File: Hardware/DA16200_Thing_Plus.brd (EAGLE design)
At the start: 22.9 x 58.4 mm, 98 parts, among them J2 THING_PLUS, J3 Qwiic, J5 USB C, J6 microSD, J7 CORTEX_JTAG_DEBUG_PTH_NS, Q1 20V/4.2A/52mΩ/1.4W, U1 DA16200MOD, U2 CH340E_MSOP10, U3 MCP73831, U5 4MB Flash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

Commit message: Checklist
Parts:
- added R20, R21: 10k, SparkFun-Resistors:0402-TIGHT
- renumbered JP2 to LED, JP3 to CHG
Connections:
- net 3.3V: now also R20.2, R21.2
- net SD_CS: now also R21.1
- net SPI_CSB: now also R20.1
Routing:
- net 3.3V: track 20.9 -> 22.4 mm, vias 12 -> 14
- net SPI_CSB: track 22.4 -> 23.7 mm
- net SD_CS: track 48.9 -> 50.0 mm
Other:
- board text added: "1"
- board text added: "2"
- board text added: "3"
- board text added: "4"
- board text added: "Four Layers"
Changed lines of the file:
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@@
 <?xml version="1.0" encoding="utf-8"?>
 <!DOCTYPE eagle SYSTEM "eagle.dtd">
-<eagle version="9.6.2">
+<eagle version="9.5.2">
 <drawing>
 <settings>
@@
 <layer number="37" name="tTest" color="7" fill="1" visible="no" active="yes"/>
 <layer number="38" name="bTest" color="7" fill="1" visible="no" active="yes"/>
-<layer number="39" name="tKeepout" color="4" fill="11" visible="no" active="yes"/>
+<layer number="39" name="tKeepout" color="4" fill="11" visible="yes" active="yes"/>
 <layer number="40" name="bKeepout" color="1" fill="11" visible="no" active="yes"/>
 <layer number="41" name="tRestrict" color="4" fill="10" visible="no" active="yes"/>
@@
 <layer number="45" name="Holes" color="7" fill="1" visible="yes" active="yes"/>
 <layer number="46" name="Milling" color="3" fill="1" visible="no" active="yes"/>
-<layer number="47" name="Measures" color="7" fill="1" visible="no" active="yes"/>
+<layer number="47" name="Measures" color="7" fill="1" visible="yes" active="yes"/>
 <layer number="48" name="Document" color="7" fill="1" visible="no" active="yes"/>
 <layer number="49" name="Reference" color="7" fill="1" visible="no" active="yes"/>
@@
 <layer number="95" name="Names" color="7" fill="1" visible="no" active="no"/>
 <layer number="96" name="Values" color="7" fill="1" visible="no" active="no"/>
-<layer number="2" name="gndvert" color="10" fill="7" visible="no" active="yes"/>
-<layer number="15" name="pwrhorz" color="4" fill="7" visible="no" active="yes"/>
+<layer number="2" name="gndvert" color="10" fill="7" visible="yes" active="yes"/>
+<layer number="15" name="pwrhorz" color="4" fill="7" visible="yes" active="yes"/>
 <layer number="3" name="Route3" color="4" fill="3" visible="no" active="no"/>
 <layer number="4" name="Route4" color="1" fill="4" visible="no" active="no"/>
@@
 <text x="8.255" y="15.24" size="1.27" layer="21" font="vector" ratio="15" rot="R90">-</text>
 <text x="13.081" y="-19.177" size="1.778" layer="51" font="vector" ratio="15">Priyanka Makin</text>
+<text x="15.24" y="55.88" size="1.778" layer="1" font="vector" ratio="15">1</text>
+<text x="16.51" y="55.88" size="1.778" layer="2" font="vector" ratio="15">2</text>
+<text x="15.24" y="53.34" size="1.778" layer="15" font="vector" ratio="15">3</text>
+<text x="17.78" y="53.34" size="1.778" layer="16" font="vector" ratio="15" rot="MR0">4</text>
+<text x="48.641" y="44.323" size="1.778" layer="51" font="vector" ratio="15">Four Layers</text>
 </plain>
 <attributes>
@@
 <attribute name="VALUE" x="4.953" y="33.02" size="0.6096" layer="27" font="vector" ratio="20" rot="R270" align="top-center"/>
 </element>
-<element name="JP2" library="SparkFun-Jumpers" package="SMT-JUMPER_2_NC_TRACE_SILK" package3d_urn="urn:adsk.eagle:package:39281/1" value="JUMPER-SMT_2_NC_TRACE_SILK" x="19.05" y="6.35" smashed="yes" rot="MR180">
+<element name="LED" library="SparkFun-Jumpers" package="SMT-JUMPER_2_NC_TRACE_SILK" package3d_urn="urn:adsk.eagle:package:39281/1" value="JUMPER-SMT_2_NC_TRACE_SILK" x="19.05" y="6.35" smashed="yes" rot="MR180">
 <attribute name="NAME" x="19.05" y="5.207" size="0.6096" layer="26" font="vector" ratio="20" rot="MR180" align="bottom-center"/>
 <attribute name="VALUE" x="19.05" y="7.493" size="0.6096" layer="28" font="vector" ratio="20" rot="MR180" align="top-center"/>
@@
 <attribute name="PROD_ID" value="RES-15550" x="19.685" y="13.724" size="1.778" layer="27" font="vector" ratio="15" rot="R90" display="off"/>
 </element>
-<element name="JP3" library="SparkFun-Jumpers" package="SMT-JUMPER_3_1-NC_TRACE_SILK" package3d_urn="urn:adsk.eagle:package:39288/1" value="JUMPER-SMT_3_1-NC_TRACE_SILK" x="12.319" y="27.178" smashed="yes" rot="MR270">
+<element name="CHG" library="SparkFun-Jumpers" package="SMT-JUMPER_3_1-NC_TRACE_SILK" package3d_urn="urn:adsk.eagle:package:39288/1" value="JUMPER-SMT_3_1-NC_TRACE_SILK" x="12.319" y="27.178" smashed="yes" rot="MR270">
 <attribute name="NAME" x="11.176" y="25.908" size="0.6096" layer="26" font="vector" ratio="20" rot="MR270" align="bottom-center"/>
 <attribute name="VALUE" x="13.462" y="25.908" size="0.6096" layer="28" font="vector" ratio="20" rot="MR270" align="top-center"/>
@@
 <element name="U$4" library="output" package="#CURR_#0" value="" x="18.288" y="23.622" smashed="yes" rot="MR0"/>
 <element name="U$5" library="output" package="##RST##0" value="" x="21.209" y="13.97" smashed="yes" rot="MR0"/>
+<element name="R20" library="SparkFun-Resistors" package="0402-TIGHT" value="10k" x="8.763" y="47.752" smashed="yes" rot="MR90">
+<attribute name="NAME" x="9.325" y="47.752" size="0.6096" layer="26" font="vector" ratio="20" rot="MR90" align="bottom-center"/>
+<attribute name="PROD_ID" value="RES-14241" x="8.763" y="47.752" size="1.778" layer="28" font="vector" ratio="15" rot="MR90" display="off"/>
+<attribute name="VALUE" x="8.201" y="47.752" size="0.6096" layer="28" font="vector" ratio="20" rot="MR90" align="top-center"/>
+</element>
+<element name="R21" library="SparkFun-Resistors" package="0402-TIGHT" value="10k" x="16.51" y="33.02" smashed="yes" rot="MR180">
+<attribute name="NAME" x="16.51" y="32.458" size="0.6096" layer="26" font="vector" ratio="20" rot="MR180" align="bottom-center"/>
+<attribute name="PROD_ID" value="RES-14241" x="16.51" y="33.02" size="1.778" layer="28" font="vector" ratio="15" rot="MR180" display="off"/>
+<attribute name="VALUE" x="16.51" y="33.582" size="0.6096" layer="28" font="vector" ratio="20" rot="MR180" align="top-center"/>
+</element>
 </elements>
 <signals>
@@
 <contactref element="J7" pad="1"/>
 <contactref element="R9" pad="1"/>
-<contactref element="JP2" pad="2"/>
+<contactref element="LED" pad="2"/>
 <polygon width="0.1778" layer="15" isolate="0.3048">
 <vertex x="0" y="0"/>
@@
 <wire x1="19.5707" y1="6.35" x2="19.5707" y2="8.3693" width="0.3048" layer="16"/>
 <wire x1="19.5707" y1="8.3693" x2="19.05" y2="8.89" width="0.3048" layer="16"/>
+<contactref element="R21" pad="2"/>
+<contactref element="R20" pad="2"/>
+<wire x1="8.763" y1="48.252" x2="8.763" y2="49.022" width="0.3048" layer="16"/>
+<via x="8.763" y="49.022" extent="1-16" drill="0.3048"/>
+<wire x1="17.01" y1="33.02" x2="17.78" y2="33.02" width="0.3048" layer="16"/>
+<via x="17.78" y="33.02" extent="1-16" drill="0.3048"/>
 </signal>
 <signal name="GND">
@@
 <signal name="N$14">
 <contactref element="U3" pad="5"/>
-<contactref element="JP3" pad="2"/>
+<contactref element="CHG" pad="2"/>
 <wire x1="14.4479" y1="24.704" x2="14.351" y2="24.8009" width="0.1778" layer="1"/>
 <wire x1="14.351" y1="24.8009" x2="14.351" y2="25.527" width="0.1778" layer="1"/>
@@
 <wire x1="2.286" y1="45.974" x2="1.27" y2="46.99" width="0.1778" layer="15"/>
 <wire x1="15.7861" y1="40.386" x2="10.033" y2="40.386" width="0.1778" layer="16"/>
+<contactref element="R20" pad="1"/>
+<wire x1="8.763" y1="45.974" x2="8.763" y2="47.252" width="0.1778" layer="16"/>
 </signal>
 <signal name="SD_CS">
@@
 <wire x1="14.9681" y1="34.163" x2="14.9681" y2="33.7872" width="0.1778" layer="16"/>
 <wire x1="14.9681" y1="33.7872" x2="14.9655" y2="33.7846" width="0.1778" layer="16"/>
-<wire x1="14.9655" y1="33.7846" x2="14.9655" y2="17.018" width="0.1778" layer="16"/>
+<wire x1="14.9655" y1="33.7846" x2="14.9655" y2="33.02" width="0.1778" layer="16"/>
+<wire x1="14.9655" y1="33.02" x2="14.9655" y2="17.018" width="0.1778" layer="16"/>
 <wire x1="14.9655" y1="17.018" x2="14.0425" y2="16.095" width="0.1778" layer="16"/>
 <wire x1="14.0425" y1="16.095" x2="6.21" y2="16.095" width="0.1778" layer="16"/>
+<contactref element="R21" pad="1"/>
+<wire x1="16.01" y1="33.02" x2="14.9655" y2="33.02" width="0.1778" layer="16"/>
 </signal>
 <signal name="GPIOC7">
@@
 <wire x1="6.858" y1="43.18" x2="5.9309" y2="44.1071" width="0.1778" layer="2"/>
 <wire x1="5.9309" y1="44.196" x2="5.9309" y2="44.1071" width="0.1778" layer="2"/>
-<wire x1="6.858" y1="43.18" x2="6.858" y2="30.099" width="0.1778" layer="2"/>
-<wire x1="6.858" y1="30.099" x2="7.747" y2="29.21" width="0.1778" layer="2"/>
+<wire x1="6.858" y1="43.18" x2="6.858" y2="31.75" width="0.1778" layer="2"/>
+<wire x1="7.747" y1="30.861" x2="6.858" y2="31.75" width="0.1778" layer="2"/>
+<wire x1="7.747" y1="30.861" x2="7.747" y2="29.21" width="0.1778" layer="2"/>
 </signal>
 <signal name="TCLK">
@@
 <wire x1="6.163" y1="43.24" x2="6.223" y2="43.18" width="0.1778" layer="1"/>
 <via x="6.223" y="43.18" extent="1-16" drill="0.3048"/>
-<wire x1="7.747" y1="27.94" x2="6.4135" y2="29.2735" width="0.1778" layer="2"/>
-<wire x1="6.4135" y1="42.9895" x2="6.4135" y2="29.2735" width="0.1778" layer="2"/>
+<wire x1="7.747" y1="27.94" x2="7.112" y2="28.575" width="0.1778" layer="2"/>
+<wire x1="7.112" y1="30.734" x2="7.112" y2="28.575" width="0.1778" layer="2"/>
+<wire x1="7.112" y1="30.734" x2="6.4135" y2="31.4325" width="0.1778" layer="2"/>
+<wire x1="6.4135" y1="42.9895" x2="6.4135" y2="31.4325" width="0.1778" layer="2"/>
 <wire x1="6.223" y1="43.18" x2="6.4135" y2="42.9895" width="0.1778" layer="2"/>
 </signal>
@@
 <signal name="N$4">
 <contactref element="D3" pad="A"/>
-<contactref element="JP2" pad="1"/>
+<contactref element="LED" pad="1"/>
 <wire x1="18.173" y1="6.35" x2="17.145" y2="6.35" width="0.1778" layer="1"/>
 <via x="17.145" y="6.35" extent="1-16" drill="0.3048"/>
@@
 </signal>
 <signal name="N$10">
-<contactref element="JP3" pad="3"/>
+<contactref element="CHG" pad="3"/>
 <contactref element="R6" pad="2"/>
 <wire x1="10.66" y1="26.162" x2="12.2936" y2="26.162" width="0.1778" layer="16"/>
@@
 </signal>
 <signal name="N$20">
-<contactref element="JP3" pad="1"/>
+<contactref element="CHG" pad="1"/>
 <contactref element="R14" pad="2"/>
 <wire x1="10.668" y1="28.194" x2="12.2936" y2="28.194" width="0.1778" layer="16"/>

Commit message: Design review
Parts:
- R13: value 200OHM-0402T-1/16W-1% -> 200
- renumbered JP4 to SHLD
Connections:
- net HDR_RTC_WAKE2: no longer C3.1, R5.2
- net RTC_PWR_KEY: now also C3.1
- net RTC_WAKE1: now also R5.2
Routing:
- net HDR_RTC_WAKE2: track 9.80 -> 4.11 mm
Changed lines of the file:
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@@
 <text x="8.255" y="15.24" size="1.27" layer="21" font="vector" ratio="15" rot="R90">-</text>
 <text x="13.081" y="-19.177" size="1.778" layer="51" font="vector" ratio="15">Priyanka Makin</text>
-<text x="15.24" y="55.88" size="1.778" layer="1" font="vector" ratio="15">1</text>
-<text x="16.51" y="55.88" size="1.778" layer="2" font="vector" ratio="15">2</text>
-<text x="15.24" y="53.34" size="1.778" layer="15" font="vector" ratio="15">3</text>
-<text x="17.78" y="53.34" size="1.778" layer="16" font="vector" ratio="15" rot="MR0">4</text>
+<text x="19.05" y="55.88" size="1.778" layer="1" font="vector" ratio="15">1</text>
+<text x="20.32" y="55.88" size="1.778" layer="2" font="vector" ratio="15">2</text>
+<text x="19.05" y="53.34" size="1.778" layer="15" font="vector" ratio="15">3</text>
+<text x="21.59" y="53.34" size="1.778" layer="16" font="vector" ratio="15" rot="MR0">4</text>
 <text x="48.641" y="44.323" size="1.778" layer="51" font="vector" ratio="15">Four Layers</text>
 </plain>
@@
 <attribute name="PROD_ID" value="RES-15238" x="12.708" y="9.652" size="1.778" layer="27" font="vector" ratio="15" display="off"/>
 </element>
-<element name="R13" library="SparkFun-Resistors" package="0402-TIGHT" value="200OHM-0402T-1/16W-1%" x="19.685" y="13.724" smashed="yes" rot="R90">
+<element name="R13" library="SparkFun-Resistors" package="0402-TIGHT" value="200" x="19.685" y="13.724" smashed="yes" rot="R90">
 <attribute name="NAME" x="18.923" y="13.724" size="0.6096" layer="25" font="vector" ratio="20" rot="R90" align="bottom-center"/>
 <attribute name="PROD_ID" value="RES-15550" x="19.685" y="13.724" size="1.778" layer="27" font="vector" ratio="15" rot="R90" display="off"/>
@@
 <attribute name="VALUE" x="15.375" y="13.462" size="0.6096" layer="27" font="vector" ratio="20" align="top-center"/>
 </element>
-<element name="JP4" library="SparkFun-Jumpers" package="SMT-JUMPER_2_NO_SILK" package3d_urn="urn:adsk.eagle:package:39279/1" value="JUMPER-SMT_2_NO_SILK" x="8.89" y="1.27" smashed="yes" rot="MR0">
+<element name="SHLD" library="SparkFun-Jumpers" package="SMT-JUMPER_2_NO_SILK" package3d_urn="urn:adsk.eagle:package:39279/1" value="JUMPER-SMT_2_NO_SILK" x="8.89" y="1.27" smashed="yes" rot="MR0">
 <attribute name="NAME" x="8.89" y="2.413" size="0.6096" layer="26" font="vector" ratio="20" rot="MR0" align="bottom-center"/>
 <attribute name="VALUE" x="8.89" y="0.127" size="0.6096" layer="28" font="vector" ratio="20" rot="MR0" align="top-center"/>
@@
 <contactref element="D5" pad="2"/>
 <contactref element="R14" pad="1"/>
-<contactref element="JP4" pad="1"/>
+<contactref element="SHLD" pad="1"/>
 <contactref element="R4" pad="2"/>
 <contactref element="R1" pad="2"/>
@@
 <wire x1="1.27" y1="39.37" x2="2.032" y2="39.37" width="0.1778" layer="16"/>
 <wire x1="6.35" y1="48.26" x2="3.429" y2="48.26" width="0.1778" layer="16"/>
+<contactref element="C3" pad="1"/>
+<wire x1="5.715" y1="33.52" x2="1.27" y2="39.37" width="0" layer="19" extent="1-1"/>
 </signal>
 <signal name="RTC_WAKE1">
@@
 <wire x1="4.7879" y1="47.2821" x2="4.83" y2="47.24" width="0.1778" layer="1"/>
 <wire x1="2.413" y1="36.83" x2="3.048" y2="37.465" width="0.1778" layer="16"/>
+<contactref element="R5" pad="2"/>
+<wire x1="1.27" y1="36.83" x2="6.858" y2="33.52" width="0" layer="19" extent="1-1"/>
 </signal>
 <signal name="HDR_RTC_WAKE2">
 <contactref element="U1" pad="14"/>
-<contactref element="R5" pad="2"/>
 <contactref element="R7" pad="2"/>
-<contactref element="C3" pad="1"/>
 <contactref element="J2" pad="8"/>
-<wire x1="5.715" y1="33.52" x2="5.842" y2="33.52" width="0.1778" layer="1"/>
-<wire x1="5.842" y1="33.52" x2="6.858" y2="33.52" width="0.1778" layer="1"/>
-<wire x1="6.858" y1="33.52" x2="8.001" y2="33.52" width="0.1778" layer="1"/>
-<wire x1="6.858" y1="33.52" x2="6.858" y2="36.168" width="0.1778" layer="1"/>
 <wire x1="6.858" y1="36.168" x2="6.93" y2="36.24" width="0.1778" layer="1"/>
 <wire x1="1.27" y1="34.29" x2="4.191" y2="34.29" width="0.1778" layer="1"/>
-<wire x1="4.961" y1="33.52" x2="5.715" y2="33.52" width="0.1778" layer="1"/>
 <wire x1="4.191" y1="34.29" x2="4.961" y2="33.52" width="0.1778" layer="1"/>
+<wire x1="6.858" y1="36.168" x2="8.001" y2="33.52" width="0" layer="19" extent="1-1"/>
+<wire x1="4.961" y1="33.52" x2="8.001" y2="33.52" width="0" layer="19" extent="1-1"/>
 </signal>
 <signal name="N$4">
@@
 <contactref element="J5" pad="SHLD3"/>
 <contactref element="J5" pad="SHLD8"/>
-<contactref element="JP4" pad="2"/>
+<contactref element="SHLD" pad="2"/>
 <wire x1="8.4836" y1="1.27" x2="8.4686" y2="1.255" width="0.1778" layer="16"/>
 <wire x1="8.4686" y1="1.255" x2="7.11" y2="1.255" width="0.1778" layer="16"/>

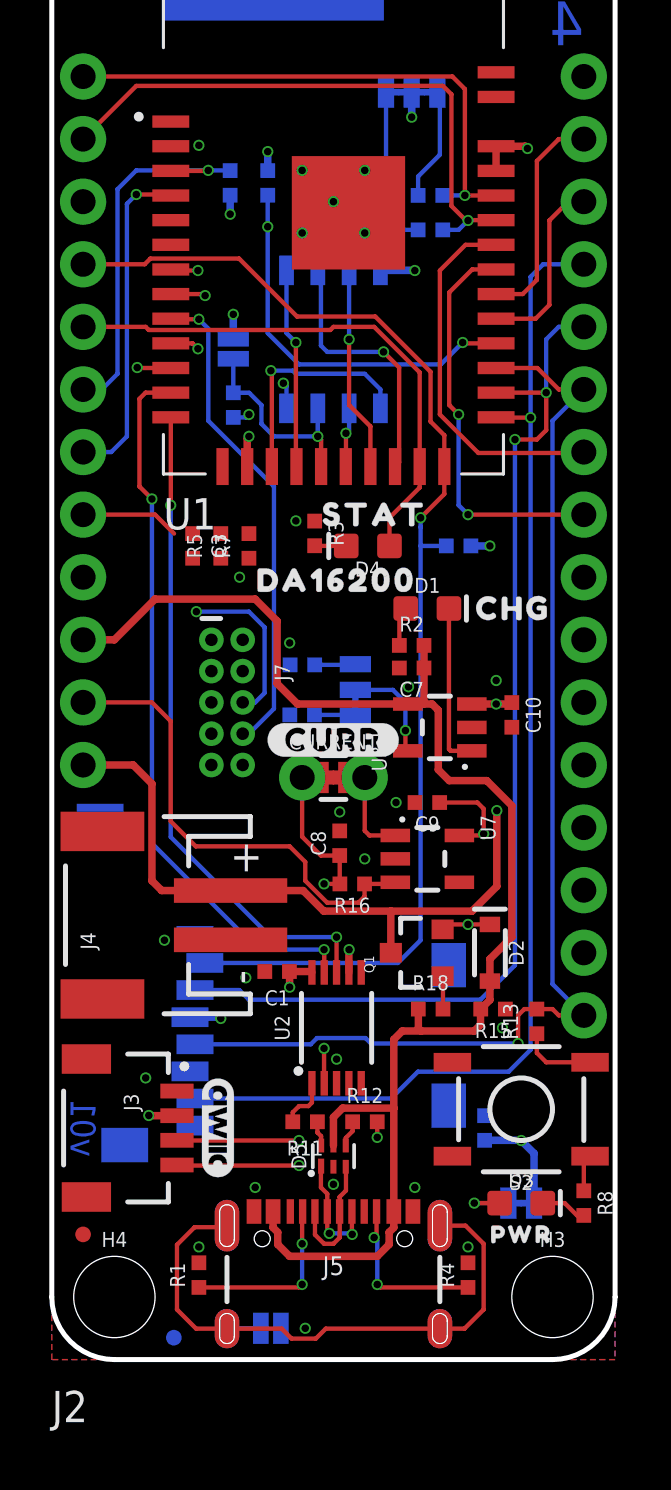
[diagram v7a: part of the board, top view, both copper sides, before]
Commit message: Design review updates
Schematic:
* Re-wire wakeup pins to match app schematic and previous designs
* Change SHLD jumper to NC
* Remove "ANT_GND" pin label from DA16200 symbol
Board:
* Draw polygon to connect shield pins of USBC connector on top and bottom
* Rename button GPIOC7
* Breakout JTAG pins to TPs on the bottom
* Redraw polygons for middle layers to avoid the antenna GND keepout
* Fixed LED label on the jumper and the pin
* Changed "CURR" label to "MEAS"
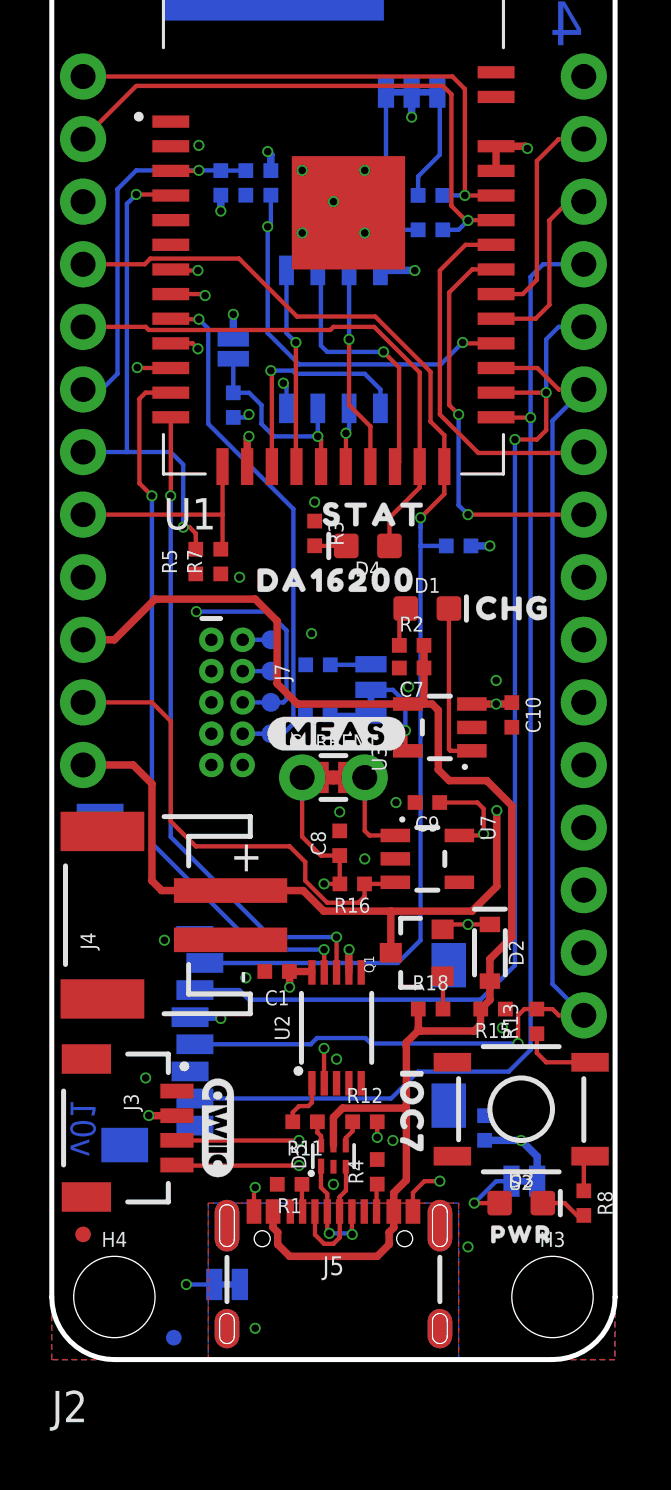
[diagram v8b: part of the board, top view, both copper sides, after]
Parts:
- removed U$4: (no value), output:#CURR_#0
- removed U$74: (no value), output:#LED#0
- added GPIO8, GPIOC7, TCLK, TMS: TEST-POINT3, SparkFun-Connectors:PAD.03X.03
- added U$6: (no value), output:IOC70
- added U$7: (no value), output:#LED_#0
- added U$8: (no value), output:#MEAS#0
- SHLD: value JUMPER-SMT_2_NO_SILK -> JUMPER-SMT_2_NC_TRACE_SILK; device SparkFun-Jumpers:SMT-JUMPER_2_NO_SILK -> SparkFun-Jumpers:SMT-JUMPER_2_NC_TRACE_SILK
- U$3: device output:#CURR#0 -> output:#MEAS_#0
- moved C3 14.9 mm to (7.87, 47.8), flipped to the bottom
- moved U$3 9.90 mm to (18.5, 23.6), flipped to the bottom
- moved R4 5.58 mm to (13.2, 7.62)
- moved R1 5.21 mm to (9.65, 7.11), turned to 180 degrees
- moved SHLD 2.51 mm to (7.11, 3.05), turned to 180 degrees
- moved U$85 2.25 mm to (13.2, 2.92)
- moved R7 1.31 mm to (6.86, 32.4)
- moved R5 1.20 mm to (5.84, 32.4)
- moved LED 0.90 mm to (19.2, 7.24)
- moved U$84 0.89 mm to (18.3, 7.24)
- moved R14 0.64 mm to (10.8, 28.2)
- moved U$88 0.64 mm to (19.6, 26.2)
- moved CHG 0.63 mm to (13.0, 27.2)
- moved R6 0.63 mm to (10.8, 26.2)
- moved U$87 0.63 mm to (19.7, 28.4)
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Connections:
- net GPIOC7: now also GPIOC7.1
- net GPIOC8: now also GPIO8.1
- net TCLK: now also TCLK.1
- net TMS: now also TMS.1
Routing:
- net N$24: track 24.5 -> 0.00 mm, vias 0 -> 1
- net RTC_WAKE1: track 13.4 -> 20.1 mm, vias 1 -> 2
- net N$11: track 7.21 -> 1.11 mm, vias 2 -> 0
- net N$12: track 6.79 -> 1.12 mm, vias 2 -> 0
- net HDR_RTC_WAKE2: track 4.11 -> 9.04 mm
- net GND: track 3.27 -> 7.44 mm
- net GPIOC7: track 18.6 -> 20.5 mm
- net GPIOC8: track 19.9 -> 21.4 mm
- net TMS: track 16.9 -> 18.0 mm
- net TCLK: track 17.3 -> 18.4 mm
- net 3.3V: track 22.4 -> 21.5 mm
- net N$14: track 4.25 -> 3.61 mm
- added copper zone on layer 1, net N$24
- added copper zone on layer 16, net N$24
